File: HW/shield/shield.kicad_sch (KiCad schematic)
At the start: 82 parts, among them J1 TRG, J2 E-STOP, J3 UART, J4 IO, J5 LDP-C BOB, J6 VIN, J7 BREAK, Q1 BSS138, Q2 BSS138, Q3 BSS138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

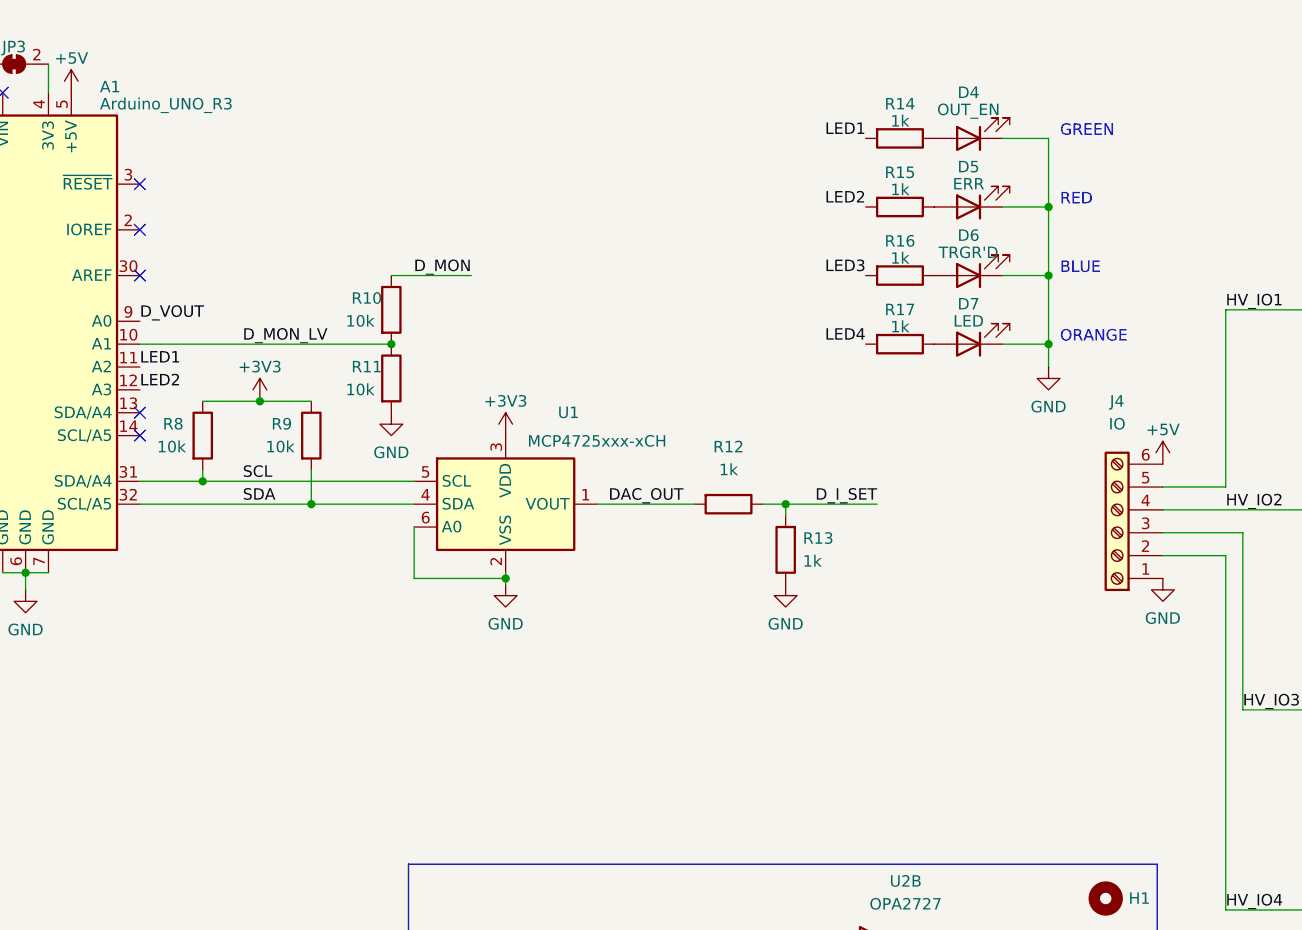
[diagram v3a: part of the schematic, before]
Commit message: fixed flipped I2C lines in the board files
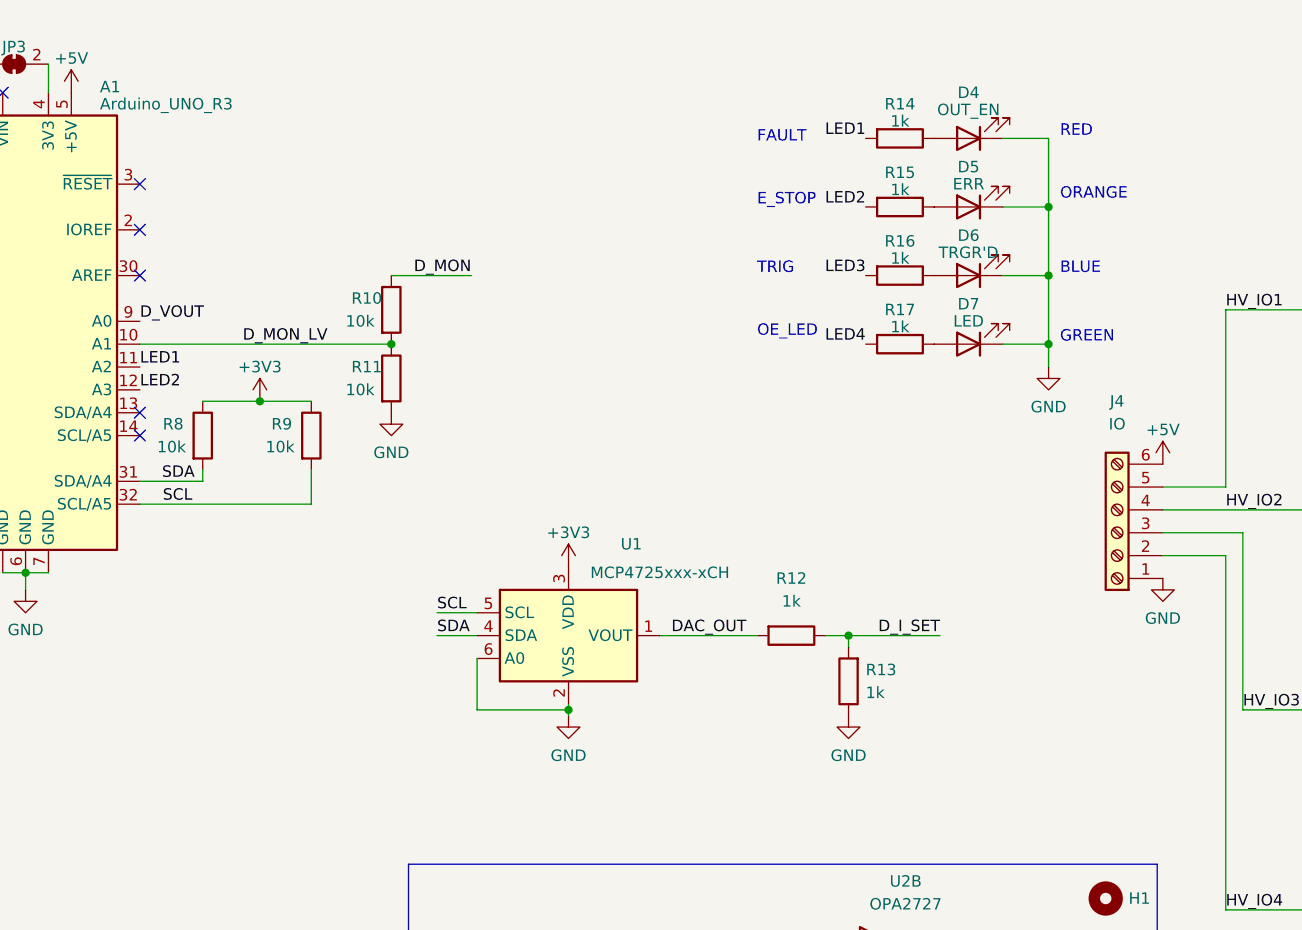
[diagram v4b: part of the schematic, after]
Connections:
- net SCL: now also A1.32 (SCL/A5), R9.2; no longer A1.31 (SDA/A4), R8.2
- net SDA: now also A1.31 (SDA/A4), R8.2; no longer A1.32 (SCL/A5), R9.2
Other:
- note added: "E_STOP"
- note added: "FAULT"
- note added: "OE_LED"
- note added: "TRIG"
- moved on the sheet: R12, R13, U1
